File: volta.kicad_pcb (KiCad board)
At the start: 2 copper layers, 79 x 100 mm, 44 parts, among them J1 AC-vivo, J10 +12, J11 -12, J12 +Vv, J13 +5V, J2 Trans-Vivo, J3 Trans-V24, J4 Trans-N24, J5 Deriv, J6 Pot_adj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

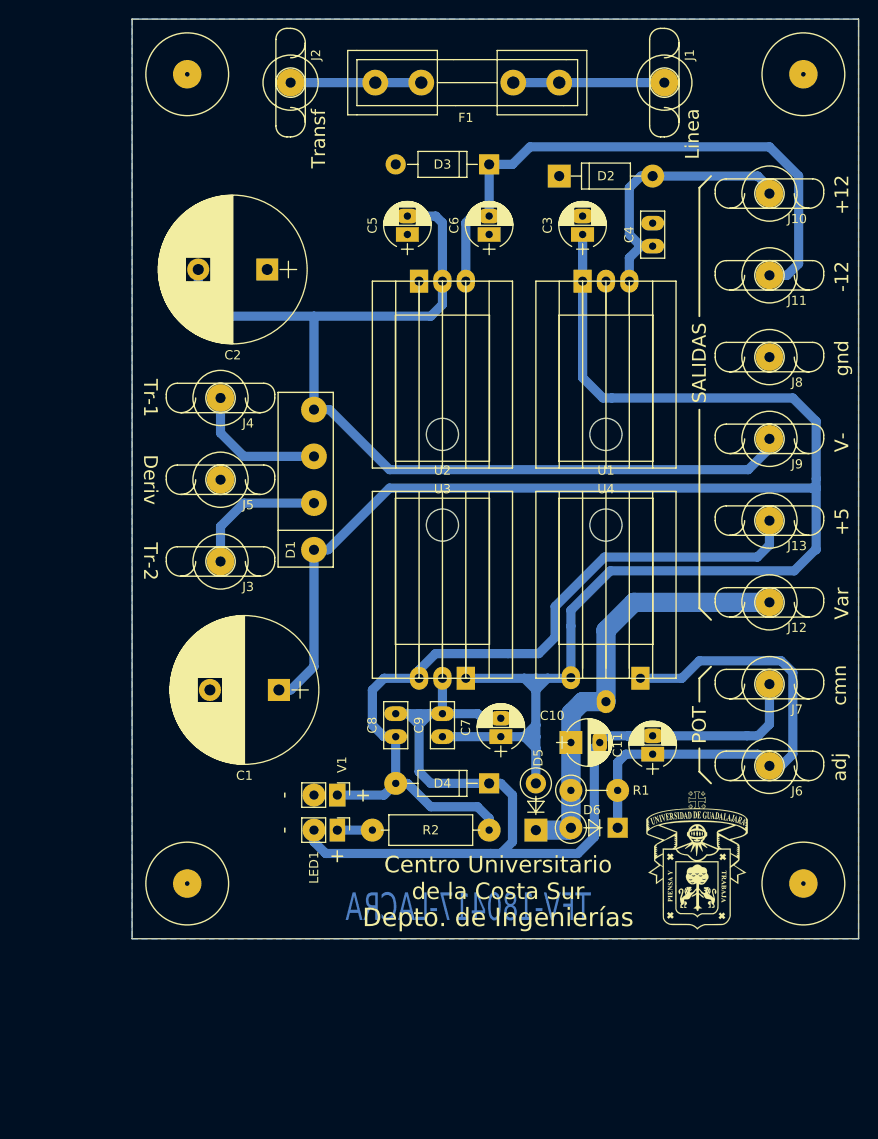
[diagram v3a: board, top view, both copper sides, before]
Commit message: Actualización mayor
cambio de pin blade 3.6
cambio de capacitores 3.3uF
cambio de pines para potenciometros
cambio de huella para fusible
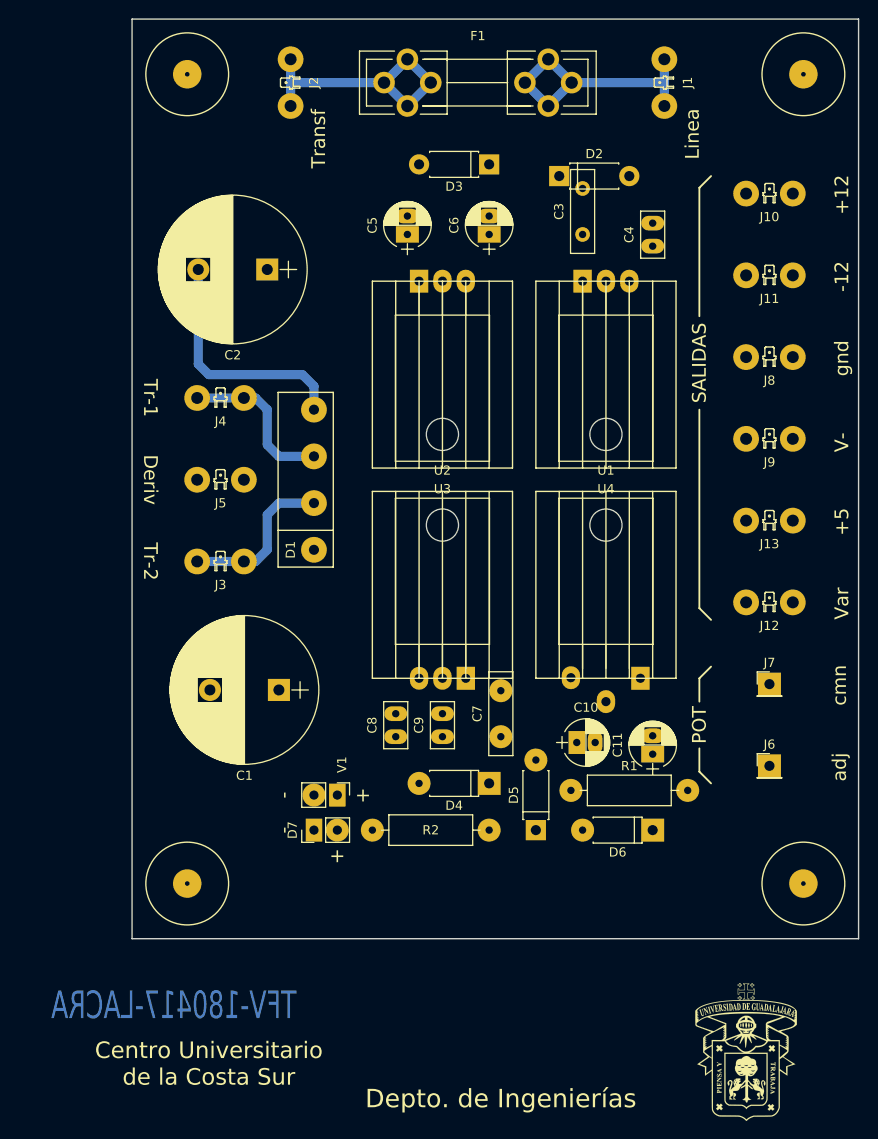
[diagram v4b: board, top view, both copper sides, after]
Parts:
- removed LED1: Activo, Pin_Headers:Pin_Header_Straight_1x02_Pitch2.54mm
- added D7: Activo, Pin_Headers:Pin_Header_Straight_1x02_Pitch2.54mm, F.Cu at (144.8, 123.2)
- C10: footprint Capacitors_THT:CP_Radial_D5.0mm_P2.50mm -> Capacitors_THT:CP_Radial_D5.0mm_P2.00mm
- C11, C6: footprint EXI_Condensadores:CP_Radial_D5.0mm_P2.00mm -> Capacitors_THT:CP_Radial_D5.0mm_P2.00mm
- C3, C7: footprint EXI_Condensadores:CP_Radial_D5.0mm_P2.00mm -> Capacitors_THT:C_Disc_D9.0mm_W2.5mm_P5.00mm
- C4, C8, C9: footprint EXI_Condensadores:C_Disc_D5.0mm_W2.5mm_P2.50mm -> Capacitors_THT:C_Disc_D5.0mm_W2.5mm_P2.50mm
- C5: value 22uF / 25V -> 22uF; footprint EXI_Condensadores:CP_Radial_D5.0mm_P2.00mm -> Capacitors_THT:CP_Radial_D5.0mm_P2.00mm
- D2, D3, D4: footprint Diodes_THT:D_DO-41_SOD81_P10.16mm_Horizontal -> Diodes_THT:D_DO-41_SOD81_P7.62mm_Horizontal
- D5, D6: footprint Diodes_THT:D_DO-41_SOD81_P5.08mm_Vertical_KathodeUp -> Diodes_THT:D_DO-41_SOD81_P7.62mm_Horizontal
- F1: footprint Fuse_Holders_and_Fuses:Fuseholder5x20_horiz_open_inline_Type-I -> Fuse_Holders_and_Fuses:Fuseholder5x20_horiz_open_universal_Type-III
- J1, J10, J11, J12, J13, J2, J3, J4, J5, J8, J9: footprint EXI_Conectores:terminal_faston_0.25 -> EXI_Conectores:blade_vertical_6.3mm_P5.08mm
- J6, J7: footprint EXI_Conectores:terminal_faston_0.25 -> Pin_Headers:Pin_Header_Straight_1x01_Pitch2.54mm
- R1: footprint Resistors_THT:R_Axial_DIN0309_L9.0mm_D3.2mm_P5.08mm_Vertical -> Resistors_THT:R_Axial_DIN0309_L9.0mm_D3.2mm_P12.70mm_Horizontal
- moved G*** 21.5 mm to (191.8, 147.3)
- moved F1 19.0 mm to (152.4, 41.9), turned to 0 degrees
- moved D6 3.82 mm to (181.6, 123.2)
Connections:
- C1 pad 1: /V+ -> +VDC
- C10 pad 2: /comun -> GNDREF
- C11 pad 2: /comun -> GNDREF
- C3 pad 1: /V+ -> +VDC
- C5 pad 2: /V- -> -VDC
- C7 pad 1: /V+ -> +VDC
- C7 pad 2: /comun -> GNDREF
- C8 pad 2: /comun -> GNDREF
- C9 pad 1: /V+ -> +VDC
- C9 pad 2: /comun -> GNDREF
- D1 pad 1: /V+ -> +VDC
- D2 pad 1: GND -> /+12
- D2 pad 2: /+12 -> GND
- D3 pad 1: /-12 -> GND
- D3 pad 2: GND -> /-12
- D4 pad 1: /comun -> /+5V
- D4 pad 2: /+5V -> GNDREF
- D5 pad 1: /+Vv -> +VDC
- D5 pad 2: /V+ -> /+Vv
- D6 pad 1: /adj -> /+Vv
- D6 pad 2: /+Vv -> /adj
- F1 pad 1: /sw -> /trans
- F1 pad 2: /trans -> /sw
- U1 pad 1: /V+ -> +VDC
- U2 pad 2: /V- -> -VDC
- U3 pad 1: /V+ -> +VDC
- U3 pad 2: /comun -> GNDREF
- U4 pad 3: /V+ -> +VDC
- V1 pad 2: GND -> GNDREF
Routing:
- net /V+: track 209.6 -> 0.00 mm
- net /comun: track 110.9 -> 0.00 mm
- net /+5V: track 86.7 -> 0.00 mm
- net /V-: track 109.1 -> 26.4 mm
- net /-12: track 63.8 -> 0.00 mm
- net /adj: track 54.3 -> 0.00 mm
- net /+Vv: track 47.5 -> 0.00 mm
- net /+12: track 29.4 -> 0.00 mm
- net /trans: track 14.2 -> 29.6 mm
- net /sw: track 16.4 -> 29.5 mm
- net Net-(D7-Pad2): track 3.81 -> 0.00 mm
- net /n24: track 15.0 -> 17.6 mm
- net /v24: track 15.0 -> 17.6 mm
- removed copper zone on B.Cu, net GND

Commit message: nuevo cajetin de udeg
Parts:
- removed D7: Activo, Pin_Headers:Pin_Header_Straight_1x02_Pitch2.54mm
- removed J6: Pot_adj, Pin_Headers:Pin_Header_Straight_1x01_Pitch2.54mm
- removed J7: Pot_gnd, Pin_Headers:Pin_Header_Straight_1x01_Pitch2.54mm
- removed V1: EXI_Ventilador, Pin_Headers:Pin_Header_Straight_1x02_Pitch2.54mm
- added G***: LOGO, EXI_Simbolgia:autlan, F.Cu at (185.4, 125.7)
- added G***: UdeG_15x20mm, EXI_Simbolgia:UdeG_15x20mm, B.Cu at (141.0, 121.3)
- added J101: Perifericos, Pin_Headers:Pin_Header_Straight_1x04_Pitch2.54mm, F.Cu at (194.5, 108.0)
- C10: footprint Capacitors_THT:CP_Radial_D5.0mm_P2.00mm -> Capacitors_THT:CP_Radial_D5.0mm_P2.50mm
- D6: footprint Diodes_THT:D_DO-41_SOD81_P7.62mm_Horizontal -> Diodes_THT:D_DO-41_SOD81_P5.08mm_Vertical_AnodeUp
- R1: footprint Resistors_THT:R_Axial_DIN0309_L9.0mm_D3.2mm_P12.70mm_Horizontal -> Resistors_THT:R_Axial_DIN0309_L9.0mm_D3.2mm_P5.08mm_Vertical
- moved G*** 54.6 mm to (142.2, 124.5)
- moved C9 14.2 mm to (172.7, 110.5), turned to 270 degrees
- moved D5 14.0 mm to (167.6, 109.2), turned to 270 degrees
- moved D4 12.7 mm to (153.7, 110.5), turned to 270 degrees
- moved D2 12.7 mm to (181.6, 59.7), turned to 90 degrees
- moved D6 11.4 mm to (172.1, 116.8), turned to 270 degrees
- moved R2 9.61 mm to (154.3, 121.9), turned to 0 degrees
- moved D3 8.98 mm to (154.9, 52.1), turned to 0 degrees
- moved C10 8.26 mm to (181.0, 116.8)
- moved C8 4.58 mm to (157.5, 110.5), turned to 270 degrees
- moved R1 4.32 mm to (176.5, 116.8), turned to 270 degrees
- moved C4 4.02 mm to (177.8, 58.4)
- moved C11 3.86 mm to (181.0, 111.1), turned to 0 degrees
- moved C7 3.59 mm to (162.6, 110.5), turned to 270 degrees
- moved C5 1.80 mm to (156.2, 57.1), turned to 270 degrees
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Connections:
- R2 pad 2: Net-(D7-Pad2) -> /LED
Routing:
- net +VDC: track 0.00 -> 174.5 mm
- net /+5V: track 0.00 -> 109.1 mm
- net GNDREF: track 0.00 -> 80.2 mm
- net /-12: track 0.00 -> 61.8 mm
- net /adj: track 0.00 -> 59.1 mm
- net /V-: track 26.4 -> 80.9 mm
- net /+Vv: track 0.00 -> 51.0 mm
- net /LED: track 0.00 -> 36.5 mm
- net /+12: track 0.00 -> 27.8 mm
- net -VDC: track 0.00 -> 5.83 mm
- added copper zone on B.Cu, net GND
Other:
- board text added: "GND"
- board text added: "LED"
- board text added: "P5k"
- board text added: "PER"
- board text added: "TFV-180428-LACRA"
- board text added: "VENT"
- board text removed: "+"
- board text removed: "-"
- board text removed: "POT"
- board text removed: "TFV-180417-LACRA"
- board text removed: "adj"
- board text removed: "cmn"

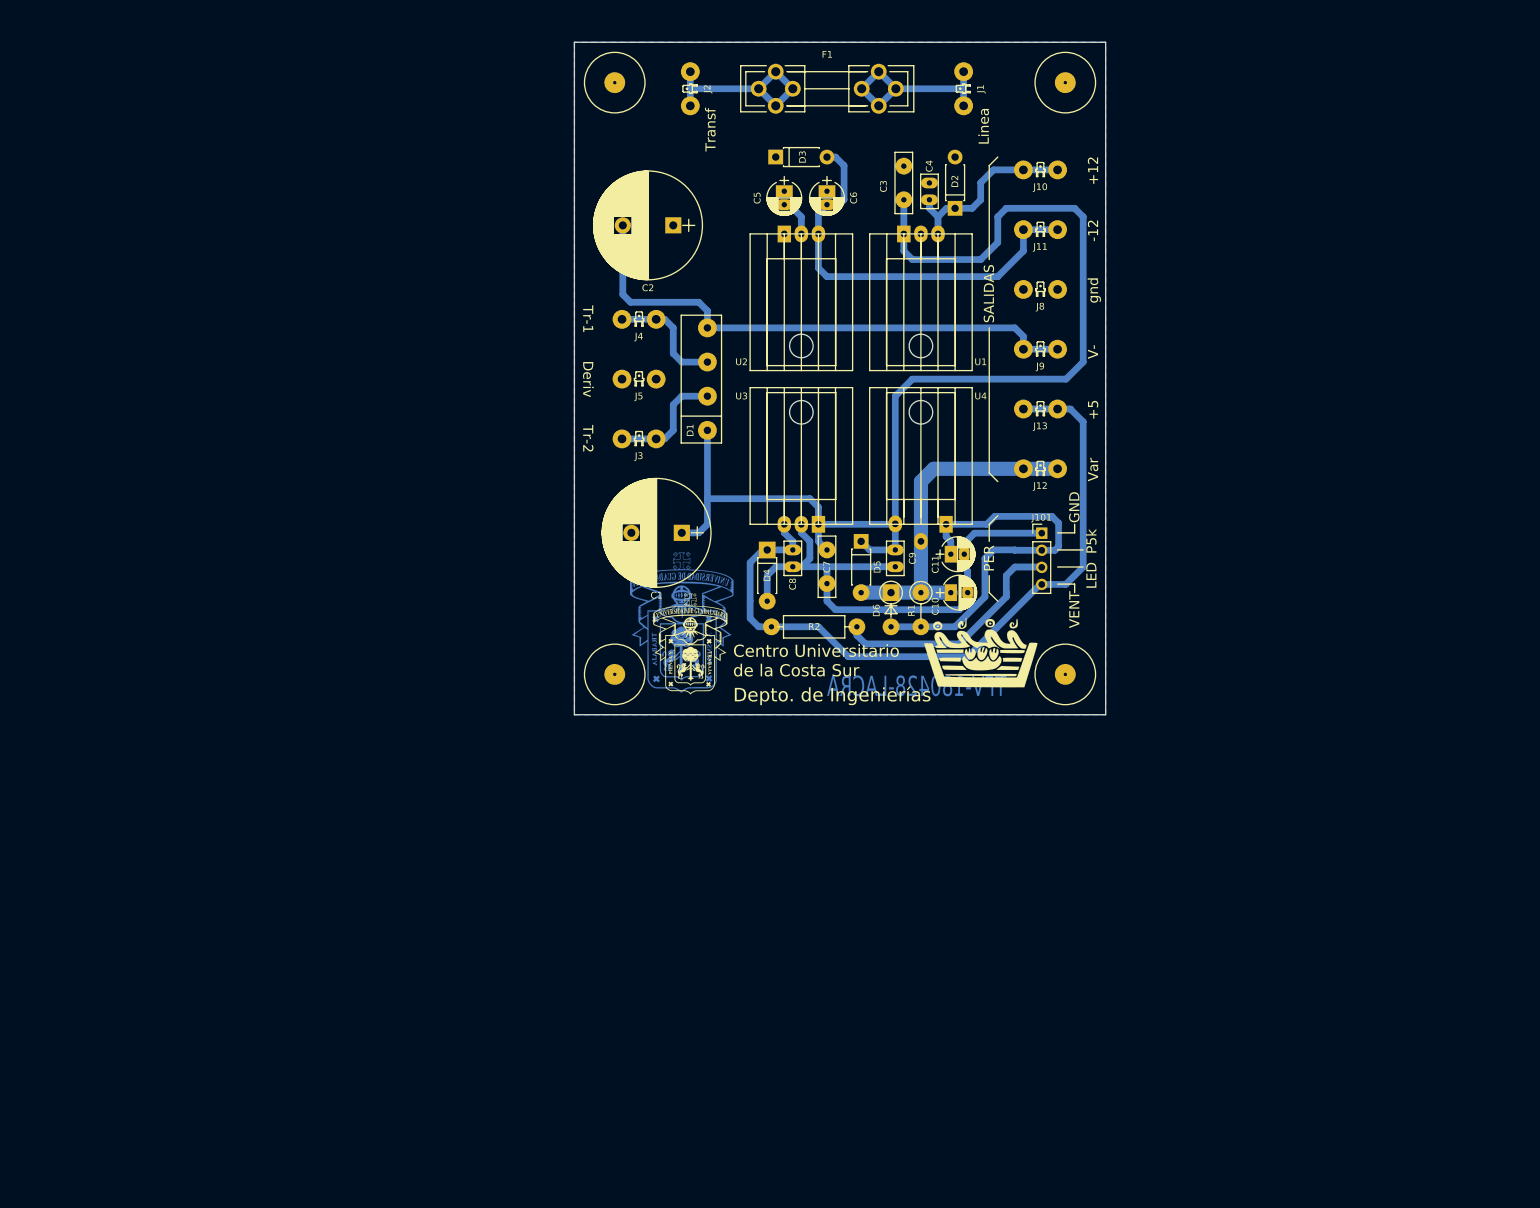
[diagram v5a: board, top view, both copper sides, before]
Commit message: avanzada en la PCB con plano de tierra
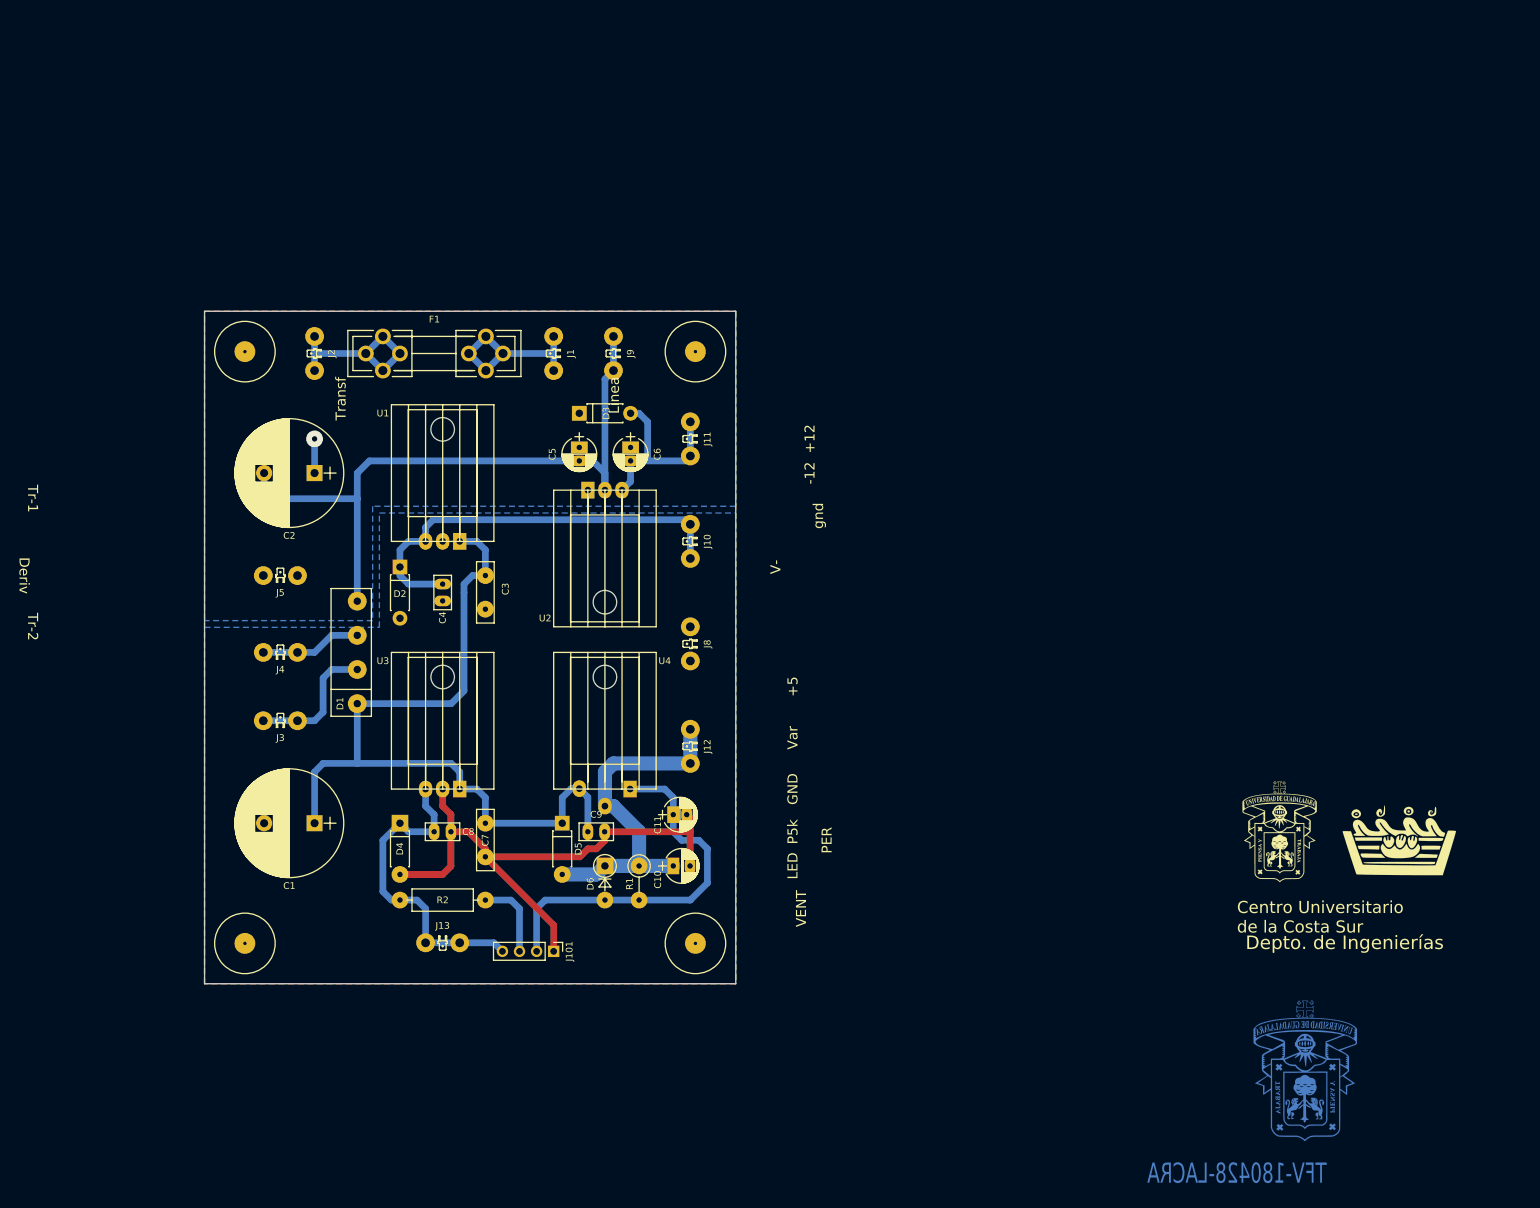
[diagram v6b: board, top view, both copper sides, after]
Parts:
- moved J13 119.2 mm to (105.4, 168.9), turned to 180 degrees
- moved G*** 114.2 mm to (233.7, 188.0)
- moved D2 98.3 mm to (99.1, 113.0), turned to 270 degrees
- moved J101 95.6 mm to (121.9, 170.2), turned to 270 degrees
- moved C4 92.2 mm to (105.4, 115.6), turned to 270 degrees
- moved G*** 92.0 mm to (229.9, 152.4)
- moved U1 84.5 mm to (105.4, 109.2), turned to 0 degrees
- moved C3 83.6 mm to (111.8, 114.3), turned to 270 degrees
- moved J10 75.9 mm to (142.2, 109.2), turned to 90 degrees
- moved J8 74.1 mm to (142.2, 124.5), turned to 90 degrees
- moved J4 72.8 mm to (81.3, 125.7)
- moved J1 72.6 mm to (121.9, 81.3)
- moved F1 70.4 mm to (94.0, 81.3)
- moved C1 69.6 mm to (86.4, 151.1)
- moved R2 68.6 mm to (99.1, 162.6)
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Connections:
- C2 pad 2: /V- -> -VDC
- D1 pad 4: /V- -> -VDC
- J9 pad 1: /V- -> -VDC
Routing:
- net -VDC: track 5.83 -> 100.3 mm
- net /V-: track 80.9 -> 0.00 mm
- net /+5V: track 109.1 -> 48.1 mm
- net +VDC: track 174.5 -> 119.5 mm
- net /+12: track 27.8 -> 62.3 mm
- net /-12: track 61.8 -> 30.1 mm
- net /LED: track 36.5 -> 12.0 mm
- net GND: track 0.00 -> 10.2 mm, vias 0 -> 2
- net GNDREF: track 80.2 -> 86.3 mm
- net /adj: track 59.1 -> 56.6 mm
- net /sw: track 29.5 -> 27.0 mm
- net /trans: track 29.6 -> 27.1 mm
- net /v24: track 17.6 -> 20.1 mm
- net /n24: track 17.6 -> 15.0 mm
- net /+Vv: track 51.0 -> 52.2 mm
- added copper zone on B.Cu, net +VDC
- added copper zone on B.Cu, net -VDC
- added copper zone on F.Cu, net GND
- removed copper zone on B.Cu, net GND
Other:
- net class Default: via_dia 2 -> 2.5
- board text removed: "SALIDAS"
